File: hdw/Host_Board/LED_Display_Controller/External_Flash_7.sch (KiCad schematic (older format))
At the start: 0 parts

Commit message: Wired Micro to external SRAM, copied Flash 8 times
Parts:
- added C?: 0.1uF, symbol LED_Display_Local_Library:C_Custom
- added C?: 10nF, symbol LED_Display_Local_Library:C_Custom
- added C?: 1nF, symbol LED_Display_Local_Library:C_Custom
- added J?: WP7, symbol Connector_Generic:Conn_02x01
- added R? (x6): 10k, symbol Custom_Library:R_Custom
- added R? (x5): 100, symbol Custom_Library:R_Custom
- added U?: SST25PF020B, Housings_SOIC:SOIC-8_3.9x4.9mm_Pitch1.27mm, symbol LED_Display_Local_Library:SST25PF020B
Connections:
- new net: R?.1, R?.2, U?.1 (~CE)
- new net: R?.1, R?.2, U?.2 (SO)
- new net: J?.1 (Pin_1), R?.2, U?.3 (~WP)
- new net: R?.1, R?.1, U?.5 (SI)
- new net: R?.1, R?.1, U?.6 (SCK)
- new net: R?.1, R?.2, U?.7 (~HOLD)
- new net +3V3: C?.1, C?.1, C?.1, R?.1, R?.1, R?.1, U?.8 (VDD)
- new net FLASH_MISO: R?.1
- new net FLASH_MOSI: R?.2
- new net FLASH_SCK: R?.2
- new net GND: C?.2, C?.2, C?.2, J?.2 (Pin_2), R?.2, R?.2, R?.2, U?.4 (VSS)
- new net ~FLASH_CE7: R?.2
- new net ~FLASH_Hold: R?.2

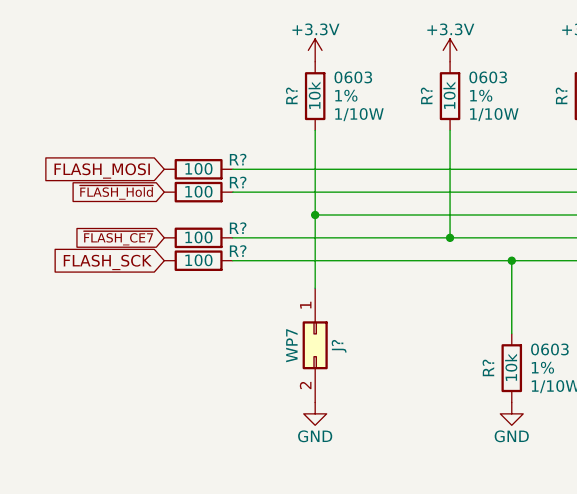
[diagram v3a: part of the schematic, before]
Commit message: Added to-do list, cleaned some pages, ~MCLR filter
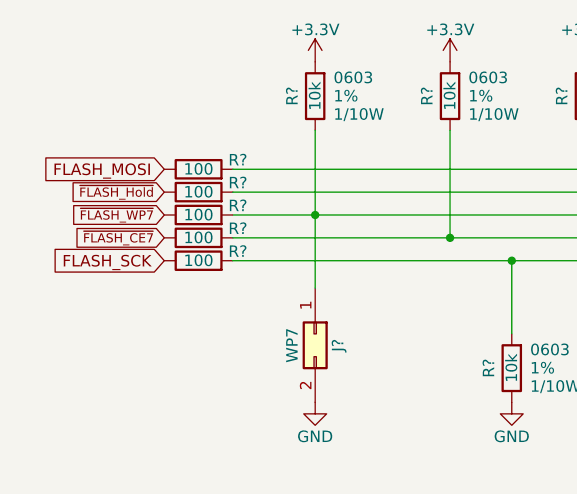
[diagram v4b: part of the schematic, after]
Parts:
- added R?: 100, symbol Custom_Library:R_Custom
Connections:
- net at J?.1 (Pin_1), R?.2, U?.3 (~WP): now also R?.1
- new net ~FLASH_WP7: R?.2
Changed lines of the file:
@@
 $Descr A 11000 8500
 encoding utf-8
-Sheet 22 25
+Sheet 20 25
 Title ""
 Date ""
@@
 AR Path="/5BB181D8/5BBEAF40" Ref="C?"  Part="1"
 AR Path="/5BB2595E/5BBEAF40" Ref="C?"  Part="1"
+AR Path="/5BB53D64/5BBEAF40" Ref="C?"  Part="1"
 F 0 "C?" H 5815 5530 50  0000 L CNN
 F 1 "0.1uF" H 5815 5330 50  0000 L CNN
@@
 AR Path="/5BB181D8/5BBEAF4B" Ref="C?"  Part="1"
 AR Path="/5BB2595E/5BBEAF4B" Ref="C?"  Part="1"
+AR Path="/5BB53D64/5BBEAF4B" Ref="C?"  Part="1"
 F 0 "C?" H 6115 5530 50  0000 L CNN
 F 1 "10nF" H 6115 5330 50  0000 L CNN
@@
 AR Path="/5BB181D8/5BBEAF56" Ref="C?"  Part="1"
 AR Path="/5BB2595E/5BBEAF56" Ref="C?"  Part="1"
+AR Path="/5BB53D64/5BBEAF56" Ref="C?"  Part="1"
 F 0 "C?" H 6415 5530 50  0000 L CNN
 F 1 "1nF" H 6415 5330 50  0000 L CNN
@@
 AR Path="/5BB181D8/5BBEAF5D" Ref="#PWR?"  Part="1"
 AR Path="/5BB2595E/5BBEAF5D" Ref="#PWR?"  Part="1"
+AR Path="/5BB53D64/5BBEAF5D" Ref="#PWR?"  Part="1"
 F 0 "#PWR?" H 6090 5410 50  0001 C CNN
 F 1 "GND" H 6090 5510 50  0000 C CNN
@@
 AR Path="/5BB181D8/5BBEAF6A" Ref="#PWR?"  Part="1"
 AR Path="/5BB2595E/5BBEAF6A" Ref="#PWR?"  Part="1"
+AR Path="/5BB53D64/5BBEAF6A" Ref="#PWR?"  Part="1"
 F 0 "#PWR?" H 6090 5050 50  0001 C CNN
 F 1 "+3.3V" H 6090 5340 50  0000 C CNN
@@
 Text GLabel 3270 3550 0    40   Input ~ 0
 ~FLASH_Hold
+$Comp
+L Custom_Library:R_Custom R?
+U 1 1 5BC1FA81
+P 3420 3650
+F 0 "R?" V 3380 3780 50  0000 L CNN
+F 1 "100" V 3420 3650 50  0000 C CNN
+F 2 "" H 3420 3650 50  0001 C CNN
+F 3 "" H 3420 3650 50  0001 C CNN
+F 4 "0603" V 3520 3650 50  0001 C CNN "display_footprint"
+F 5 "1%" V 3620 3650 50  0001 C CNN "Tolerance"
+F 6 "1/10W" V 3720 3650 50  0001 C CNN "Wattage"
+F 7 "PN" H 3720 4050 60  0001 C CNN "Digi-Key PN"
+	1    3420 3650
+	0    1    1    0
+$EndComp
+Wire Wire Line
+	3570 3650 3930 3650
+Text GLabel 3270 3650 0    40   Input ~ 0
+~FLASH_WP7
 $EndSCHEMATC

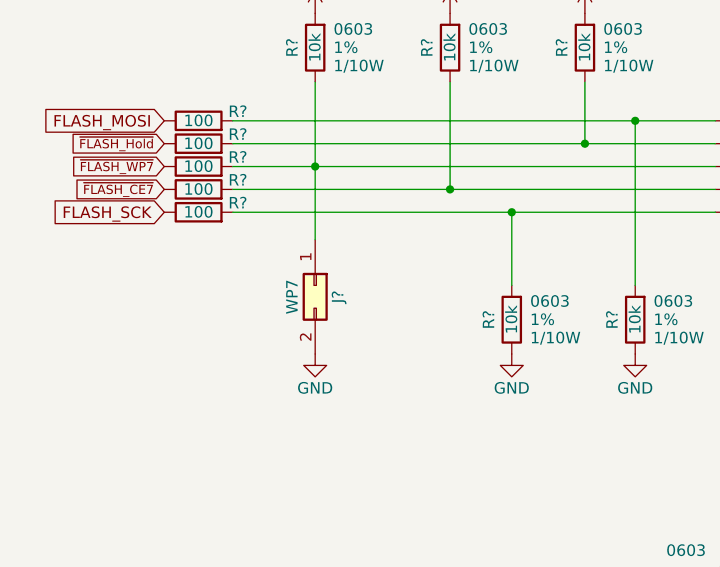
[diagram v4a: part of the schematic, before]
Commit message: Converted to KiCad 5.0.1 project, resolved library issues, cleaned up a few sheets
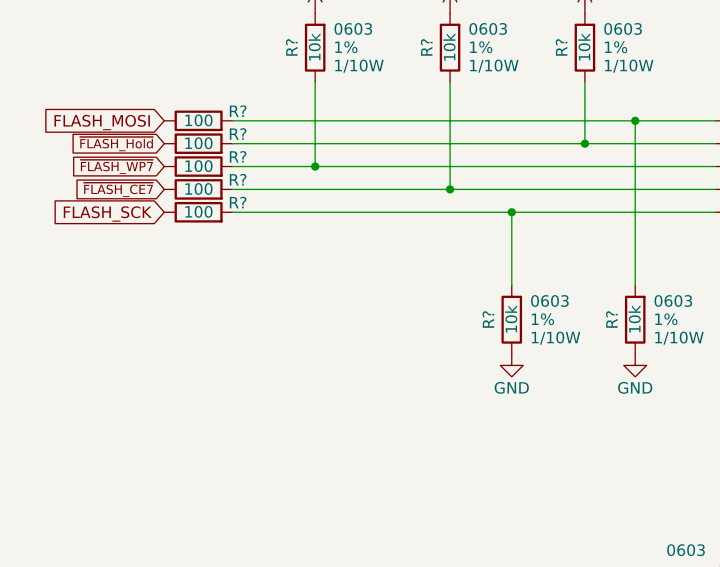
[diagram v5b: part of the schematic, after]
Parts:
- removed J?: WP7, symbol Connector_Generic:Conn_02x01
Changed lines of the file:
@@
 $Descr A 11000 8500
 encoding utf-8
-Sheet 20 25
+Sheet 19 25
 Title ""
 Date ""
@@
 F 3 "" H 6080 4050 50  0001 C CNN
 	1    6080 4050
-	1    0    0    -1
-$EndComp
-$Comp
-L Custom_Library:+3.3V #PWR?
-U 1 1 5BBEAE93
-P 6080 3250
-F 0 "#PWR?" H 6080 3100 50  0001 C CNN
-F 1 "+3.3V" H 6080 3390 50  0000 C CNN
-F 2 "" H 6080 3250 50  0000 C CNN
-F 3 "" H 6080 3250 50  0000 C CNN
-	1    6080 3250
 	1    0    0    -1
 $EndComp
@@
 $EndComp
 $Comp
-L Custom_Library:+3.3V #PWR?
-U 1 1 5BBEAEED
-P 5110 2980
-F 0 "#PWR?" H 5110 2830 50  0001 C CNN
-F 1 "+3.3V" H 5110 3120 50  0000 C CNN
-F 2 "" H 5110 2980 50  0000 C CNN
-F 3 "" H 5110 2980 50  0000 C CNN
-	1    5110 2980
-	1    0    0    -1
-$EndComp
-$Comp
-L Custom_Library:+3.3V #PWR?
-U 1 1 5BBEAEF3
-P 4520 2980
-F 0 "#PWR?" H 4520 2830 50  0001 C CNN
-F 1 "+3.3V" H 4520 3120 50  0000 C CNN
-F 2 "" H 4520 2980 50  0000 C CNN
-F 3 "" H 4520 2980 50  0000 C CNN
-	1    4520 2980
-	1    0    0    -1
-$EndComp
-$Comp
-L Custom_Library:+3.3V #PWR?
-U 1 1 5BBEAEF9
-P 3930 2980
-F 0 "#PWR?" H 3930 2830 50  0001 C CNN
-F 1 "+3.3V" H 3930 3120 50  0000 C CNN
-F 2 "" H 3930 2980 50  0000 C CNN
-F 3 "" H 3930 2980 50  0000 C CNN
-	1    3930 2980
-	1    0    0    -1
-$EndComp
-$Comp
 L Custom_Library:R_Custom R?
 U 1 1 5BBEAF03
@@
 Wire Wire Line
 	3930 3650 5680 3650
-$Comp
-L Connector_Generic:Conn_02x01 J?
-U 1 1 5BBEAF1A
-P 3930 4170
-AR Path="/5BB2595E/5BBEAF1A" Ref="J?"  Part="1"
-AR Path="/5BB53D64/5BBEAF1A" Ref="J?"  Part="1"
-F 0 "J?" H 3980 4270 50  0000 C CNN
-F 1 "WP7" H 3980 4070 50  0000 C CNN
-F 2 "" H 3930 4170 50  0001 C CNN
-F 3 "~" H 3930 4170 50  0001 C CNN
-	1    3930 4170
-	0    1    1    0
-$EndComp
-Wire Wire Line
-	3930 3970 3930 3650
 Connection ~ 3930 3650
-$Comp
-L power:GND #PWR?
-U 1 1 5BBEAF23
-P 3930 4470
-F 0 "#PWR?" H 3930 4220 50  0001 C CNN
-F 1 "GND" H 3930 4320 50  0000 C CNN
-F 2 "" H 3930 4470 50  0001 C CNN
-F 3 "" H 3930 4470 50  0001 C CNN
-	1    3930 4470
-	1    0    0    -1
-$EndComp
 Text GLabel 3270 3450 0    50   Input ~ 0
 FLASH_MOSI
@@
 Text GLabel 3270 3650 0    40   Input ~ 0
 ~FLASH_WP7
+$Comp
+L power:+3.3V #PWR?
+U 1 1 5BDFB78E
+P 6080 3250
+F 0 "#PWR?" H 6080 3100 50  0001 C CNN
+F 1 "+3.3V" H 6080 3390 50  0000 C CNN
+F 2 "" H 6080 3250 50  0001 C CNN
+F 3 "" H 6080 3250 50  0001 C CNN
+	1    6080 3250
+	1    0    0    -1
+$EndComp
+$Comp
+L power:+3.3V #PWR?
+U 1 1 5BDFB7C2
+P 5110 2980
+F 0 "#PWR?" H 5110 2830 50  0001 C CNN
+F 1 "+3.3V" H 5110 3120 50  0000 C CNN
+F 2 "" H 5110 2980 50  0001 C CNN
+F 3 "" H 5110 2980 50  0001 C CNN
+	1    5110 2980
+	1    0    0    -1
+$EndComp
+$Comp
+L power:+3.3V #PWR?
+U 1 1 5BDFB833
+P 4520 2980
+F 0 "#PWR?" H 4520 2830 50  0001 C CNN
+F 1 "+3.3V" H 4520 3120 50  0000 C CNN
+F 2 "" H 4520 2980 50  0001 C CNN
+F 3 "" H 4520 2980 50  0001 C CNN
+	1    4520 2980
+	1    0    0    -1
+$EndComp
+$Comp
+L power:+3.3V #PWR?
+U 1 1 5BDFB860
+P 3930 2980
+F 0 "#PWR?" H 3930 2830 50  0001 C CNN
+F 1 "+3.3V" H 3930 3120 50  0000 C CNN
+F 2 "" H 3930 2980 50  0001 C CNN
+F 3 "" H 3930 2980 50  0001 C CNN
+	1    3930 2980
+	1    0    0    -1
+$EndComp
 $EndSCHEMATC

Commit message: rage commit
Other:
- note added: "24. External FLASH 7"
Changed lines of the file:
@@
 $Descr A 11000 8500
 encoding utf-8
-Sheet 19 31
+Sheet 24 31
 Title ""
 Date ""
@@
 $EndComp
 $Comp
-L power:GND #PWR?
+L power:GND #PWR0283
 U 1 1 5BBEAE8D
 P 6080 4050
-F 0 "#PWR?" H 6080 3800 50  0001 C CNN
+F 0 "#PWR0283" H 6080 3800 50  0001 C CNN
 F 1 "GND" H 6080 3900 50  0000 C CNN
 F 2 "" H 6080 4050 50  0001 C CNN
@@
 $EndComp
 $Comp
-L power:GND #PWR?
+L power:GND #PWR0284
 U 1 1 5BBEAEDB
 P 4790 4470
-F 0 "#PWR?" H 4790 4220 50  0001 C CNN
+F 0 "#PWR0284" H 4790 4220 50  0001 C CNN
 F 1 "GND" H 4790 4320 50  0000 C CNN
 F 2 "" H 4790 4470 50  0001 C CNN
@@
 $EndComp
 $Comp
-L power:GND #PWR?
+L power:GND #PWR0285
 U 1 1 5BBEAEE1
 P 5330 4470
-F 0 "#PWR?" H 5330 4220 50  0001 C CNN
+F 0 "#PWR0285" H 5330 4220 50  0001 C CNN
 F 1 "GND" H 5330 4320 50  0000 C CNN
 F 2 "" H 5330 4470 50  0001 C CNN
@@
 $EndComp
 $Comp
-L power:GND #PWR?
+L power:GND #PWR0286
 U 1 1 5BBEAEE7
 P 6750 4000
-F 0 "#PWR?" H 6750 3750 50  0001 C CNN
+F 0 "#PWR0286" H 6750 3750 50  0001 C CNN
 F 1 "GND" H 6750 3850 50  0000 C CNN
 F 2 "" H 6750 4000 50  0001 C CNN
@@
 AR Path="/5BB181D8/5BBEAF5D" Ref="#PWR?"  Part="1"
 AR Path="/5BB2595E/5BBEAF5D" Ref="#PWR?"  Part="1"
-AR Path="/5BB53D64/5BBEAF5D" Ref="#PWR?"  Part="1"
-F 0 "#PWR?" H 6090 5410 50  0001 C CNN
+AR Path="/5BB53D64/5BBEAF5D" Ref="#PWR0287"  Part="1"
+F 0 "#PWR0287" H 6090 5410 50  0001 C CNN
 F 1 "GND" H 6090 5510 50  0000 C CNN
 F 2 "" H 6090 5660 50  0001 C CNN
@@
 AR Path="/5BB181D8/5BBEAF6A" Ref="#PWR?"  Part="1"
 AR Path="/5BB2595E/5BBEAF6A" Ref="#PWR?"  Part="1"
-AR Path="/5BB53D64/5BBEAF6A" Ref="#PWR?"  Part="1"
-F 0 "#PWR?" H 6090 5050 50  0001 C CNN
+AR Path="/5BB53D64/5BBEAF6A" Ref="#PWR0288"  Part="1"
+F 0 "#PWR0288" H 6090 5050 50  0001 C CNN
 F 1 "+3.3V" H 6090 5340 50  0000 C CNN
 F 2 "" H 6090 5200 50  0001 C CNN
@@
 ~FLASH_WP7
 $Comp
-L power:+3.3V #PWR?
+L power:+3.3V #PWR0289
 U 1 1 5BDFB78E
 P 6080 3250
-F 0 "#PWR?" H 6080 3100 50  0001 C CNN
+F 0 "#PWR0289" H 6080 3100 50  0001 C CNN
 F 1 "+3.3V" H 6080 3390 50  0000 C CNN
 F 2 "" H 6080 3250 50  0001 C CNN
@@
 $EndComp
 $Comp
-L power:+3.3V #PWR?
+L power:+3.3V #PWR0290
 U 1 1 5BDFB7C2
 P 5110 2980
-F 0 "#PWR?" H 5110 2830 50  0001 C CNN
+F 0 "#PWR0290" H 5110 2830 50  0001 C CNN
 F 1 "+3.3V" H 5110 3120 50  0000 C CNN
 F 2 "" H 5110 2980 50  0001 C CNN
@@
 $EndComp
 $Comp
-L power:+3.3V #PWR?
+L power:+3.3V #PWR0291
 U 1 1 5BDFB833
 P 4520 2980
-F 0 "#PWR?" H 4520 2830 50  0001 C CNN
+F 0 "#PWR0291" H 4520 2830 50  0001 C CNN
 F 1 "+3.3V" H 4520 3120 50  0000 C CNN
 F 2 "" H 4520 2980 50  0001 C CNN
@@
 $EndComp
 $Comp
-L power:+3.3V #PWR?
+L power:+3.3V #PWR0292
 U 1 1 5BDFB860
 P 3930 2980
-F 0 "#PWR?" H 3930 2830 50  0001 C CNN
+F 0 "#PWR0292" H 3930 2830 50  0001 C CNN
 F 1 "+3.3V" H 3930 3120 50  0000 C CNN
 F 2 "" H 3930 2980 50  0001 C CNN
@@
 	1    0    0    -1
 $EndComp
+$Comp
+L Graphic:SYM_ESD_Large #SYM?
+U 1 1 5C02ECCC
+P 6490 4500
+AR Path="/5BAAE0FA/5C02ECCC" Ref="#SYM?"  Part="1"
+AR Path="/5BB182B1/5C02ECCC" Ref="#SYM?"  Part="1"
+AR Path="/5BB53D64/5C02ECCC" Ref="#SYM?"  Part="1"
+F 0 "#SYM?" H 6490 4700 50  0001 C CNN
+F 1 "SYM_ESD_Large" H 6490 4250 50  0001 C CNN
+F 2 "" H 6485 4470 50  0001 C CNN
+F 3 "~" H 6485 4470 50  0001 C CNN
+	1    6490 4500
+	1    0    0    -1
+$EndComp
+Text Notes 550  700  0    100  ~ 20
+24. External FLASH 7
+$Comp
+L LED_Display_Local_Library:MU_Logo #G?
+U 1 1 5BFFDF04
+P 9900 1100
+F 0 "#G?" H 9900 614 60  0001 C CNN
+F 1 "MU_Logo" H 9900 1586 60  0001 C CNN
+F 2 "" H 9900 1100 50  0001 C CNN
+F 3 "" H 9900 1100 50  0001 C CNN
+	1    9900 1100
+	1    0    0    -1
+$EndComp
